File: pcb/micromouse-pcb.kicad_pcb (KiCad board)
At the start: 4 copper layers, 100 x 120 mm, 179 parts, among them J1 BATT_IN_2S, J5 MOTOR_A_N20_ENCODER, J6 MOTOR_B_N20_ENCODER, J7 USB-C rear (GCT USB4105; VBUS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, J8 JTAG_1x6 (3V3,TMS,TCK,TDO,TDI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, J9 BALANCE_2S, Q1 Q_PMOS reverse guard (DMP3098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, Q16 BSS138 (real part; Q_NMOS_GSD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, Q17 BSS138 (real part; Q_NMOS_GSD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, Q18 BSS138 (real part; Q_NMOS_GSD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, Q19 BSS138 (real part; Q_NMOS_GSD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, Q2 PT334-6B (5mm filtered PT; LO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, Q20 BSS138 (real part; Q_NMOS_GSD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, Q21 BSS138 (real part; Q_NMOS_GSD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, Q22 BSS138 (real part; Q_NMOS_GSD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, Q23 BSS138 (real part; Q_NMOS_GSD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, Q24 BSS138 (real part; Q_NMOS_GSD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, Q25 BSS138 (real part; Q_NMOS_GSD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, Q26 BSS138 (real part; Q_NMOS_GSD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, Q27 BSS138 (real part; Q_NMOS_GSD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, Q28 BSS84 (PMOS indicator driver;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, Q29 BSS84 (PMOS indicator driver;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, Q3 PT334-6B (5mm filtered PT; LO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, Q30 BSS84 (PMOS indicator driver;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, Q31 BSS84 (PMOS indicator driver;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, Q32 BSS84 (PMOS indicator driver;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, Q33 BSS84 (PMOS indicator driver;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, Q4 PT334-6B (5mm filtered PT; LO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, Q5 PT334-6B (5mm filtered PT; LO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, Q6 PT334-6B (5mm filtered PT; LO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, Q7 PT334-6B (5mm filtered PT; LO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, SW1 BTN_A (start / BOOT), SW2 RESET, SW3 BTN_B, SW4 BTN_C, SW5 PWR ALL (PCM12SMTR slide; sli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, SW6 PWR MOTORS (PCM12SMTR slide; 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, U1 AP63203WU-7 (fixed 3.3V 2A bu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, U2 TB6612FNG, U3 ESP32-S3-WROOM-1-N8R2 (quad P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, U4 CD74HC4067M, U6 USBLC6-2SC6 (SOT-23-6; 2P6 ba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, U7 TPS54302DDCR (6.0V/3A motor b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, U8 BNO055 (9-axis IMU + fusion; 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

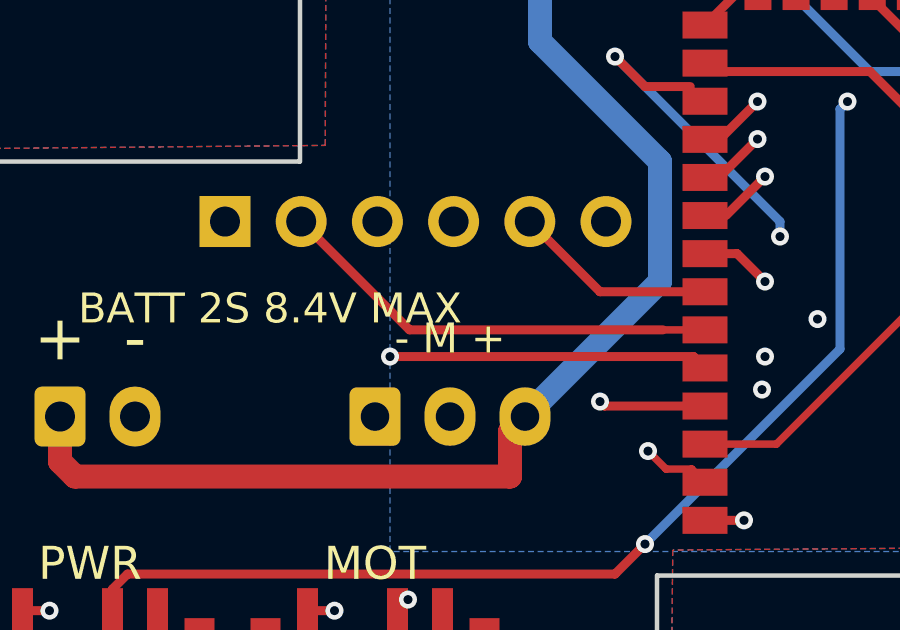
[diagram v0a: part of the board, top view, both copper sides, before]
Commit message: Silk: J9 polarity text clear of BATT label; schematic fuse MPN synced (parity 0)
Co-Authored-By: Claude Opus 4.8 (1M context) <noreply@anthropic.com>
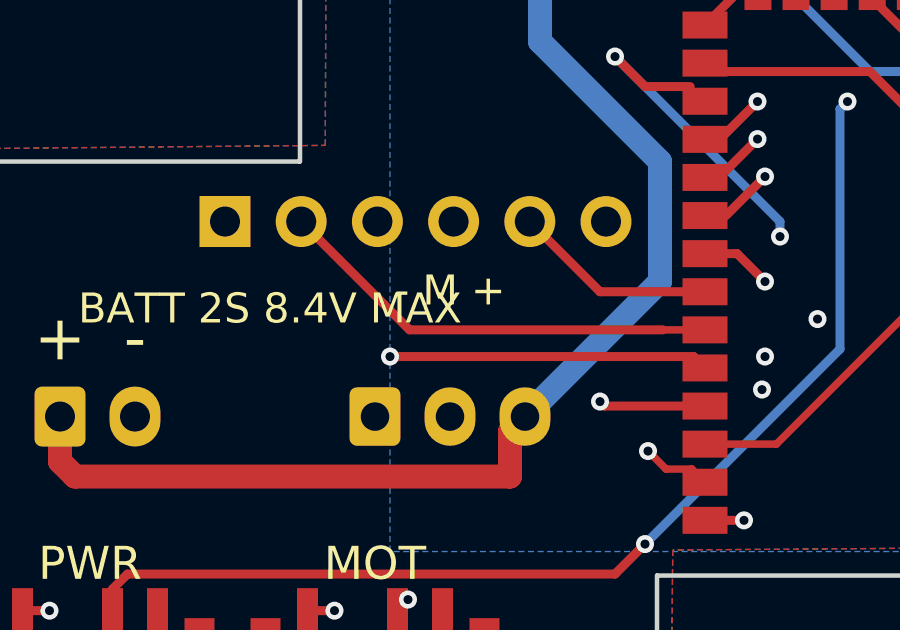
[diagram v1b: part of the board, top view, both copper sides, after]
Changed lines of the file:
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@@
 	)
 	(gr_text "- M +"
-		(at 18 105.9 0)
+		(at 18 104.3 0)
 		(layer "F.SilkS")
 		(effects (font (size 1 1) (thickness 0.2)))

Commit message: Silk: drop the J9 '- M +' text (keyed connector; crowded label zone) -- verify_drc PASS again
Co-Authored-By: Claude Opus 4.8 (1M context) <noreply@anthropic.com>
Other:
- board text removed: "- M +"
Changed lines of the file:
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@@
 		(effects (font (size 1.5 1.5) (thickness 0.3)))
 	)
-	(gr_text "- M +"
-		(at 18 104.3 0)
-		(layer "F.SilkS")
-		(effects (font (size 1 1) (thickness 0.2)))
-	)
 )

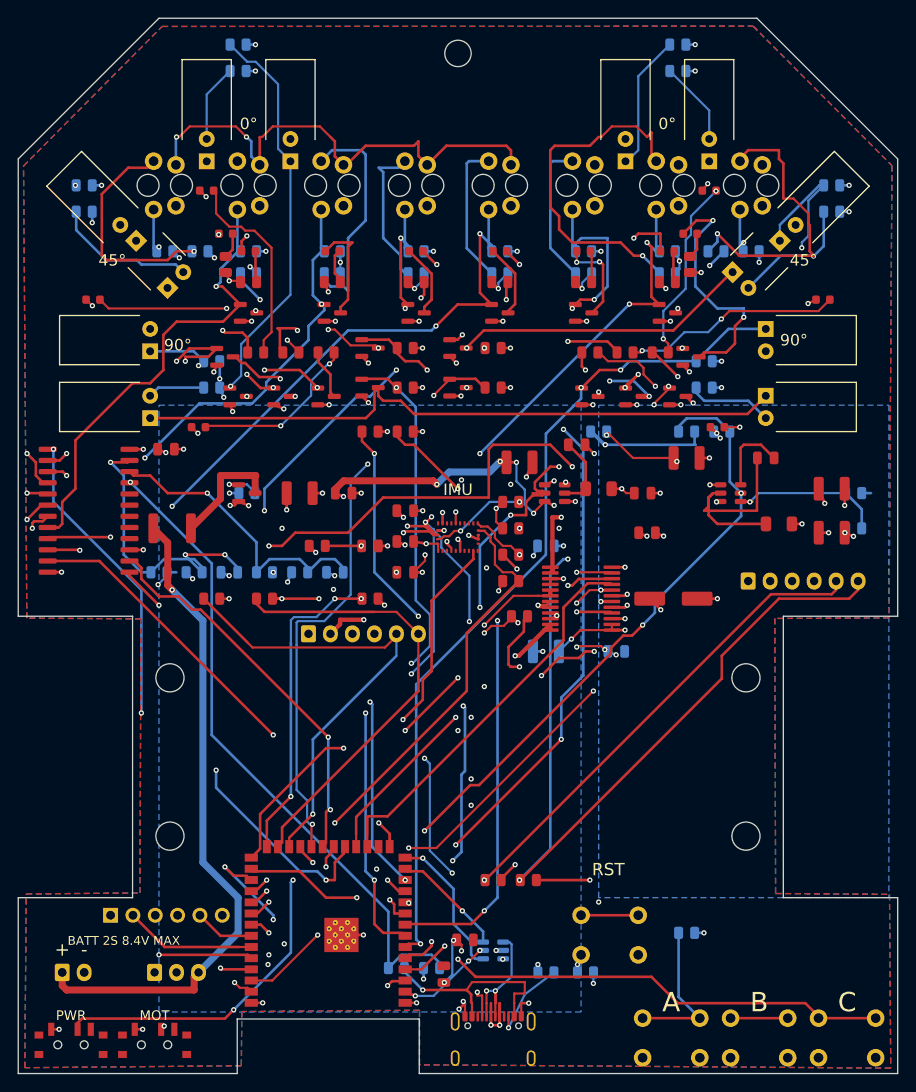
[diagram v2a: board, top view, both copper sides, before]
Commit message: Rev 7.2: XT60 + buzzer + ZH direct-plug motors + IMU self-test -- verify_drc 0/0, 12/12 battery, dual fab packages
User work order (HANDOFF 18) + same-day requests, all closed:
- J10 AMASS XT60-M (male) battery input in PARALLEL with J1 JST-XH:
  rear-right shelf placement via hole-aware free-rect scan against the
  true Edge.Cuts polygon with optical-corridor keepouts (two earlier
  candidate spots rejected with evidence: outline void / line-array
  through-holes). 0.8mm BATT_RAW feed; '+'/'-' + ONE PACK ONLY silk;
  normal BOM line (Lion procures; hand-fit fallback documented).
- BZ1 buzzer (CMT-8504, 15R coil) on IO46 via R81 220R -> Q34 MMBT2222A
  + D29 1N4148W flyback; strap-safe (load only ever pulls the boot strap
  low). fw beep API: ready/run/stop/low-batt/stall/IMU-fail chirps.
- J5/J6 -> JST ZH B6B-ZR in the robu GA12-N20 factory-cable order
  (M1,VCC,C1,C2,GND,M2): motor plugs straight in, zero soldering.
  Meter-check VCC/GND (pins 2/5) once before first plug-in.
- J9 balance lead now OPTIONAL: fw auto-detects (BAT_MID_SENSE ~0V) and
  falls back to the 6.6V pack floor.
- IMU functioning checks: sim_preflight I1-I6 (bus topology, Fast-mode
  timing, straps, reset pull-ups, CAP, INT, register audit) + boot
  self-test in fw (CHIP_ID, POST, fusion status; 4-chirp on failure).
- Sims updated to the exact ordered motor (600 ticks/rev, 200RPM, 43mm
  wheel, 0.23A stall); 8.4V question closed: motors sit on the regulated
  6.00V rail (circuit_tests M2/M3).
- Selective silk refdes for 23 debug-critical parts (clear-spot scanner
  seeded against board labels) + assembly-top/bottom.pdf debug maps
  (new export_fab gate). Project-local 3D models for ZH + buzzer.
- Production folders (pcb/tools/export_release.py): fab_release/
  lion-circuits/ (gerber zip + BOM + pos + assembly PDFs + ORDERING.md)
  and fab_release/jlcpcb/ (flat gerber+drill zip, JLC-format BOM/CPL,
  ORDERING.md with LCSC/rotation/origin caveats).
- Full Lion stock re-sweep 2026-07-19/20: every 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
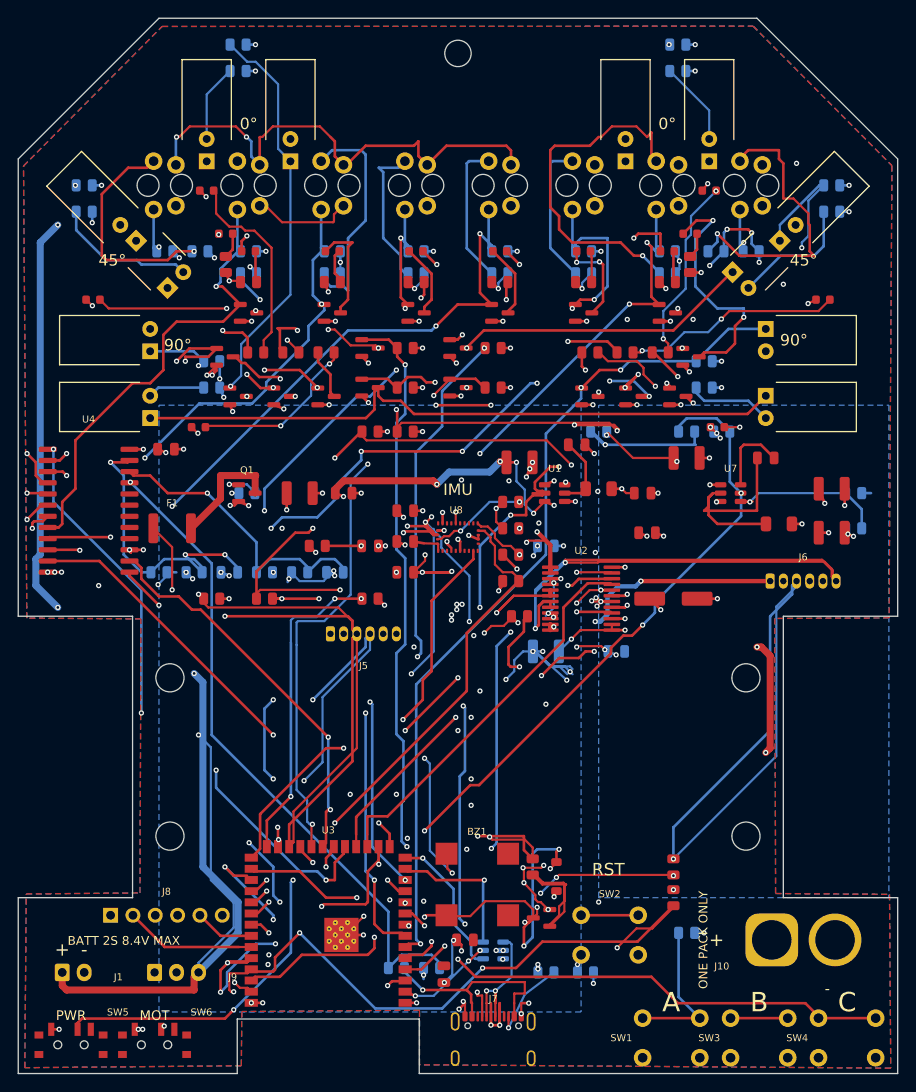
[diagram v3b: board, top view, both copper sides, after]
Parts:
- added BZ1: CMT-8504-100-SMT (magnetic transducer 8.5mm, 15R coil, 4kHz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, Buzzer_Beeper:MagneticBuzzer_CUI_CMT-8504-100-SMT, F.Cu at (52.2, 98.5)
- added D29: 1N4148W (flyback clamp across the buzzer coil), Diode_SMD:D_SOD-123, F.Cu at (61.2, 97.6)
- added J10: BATT_IN_XT60 (parallel option -- ONE PACK ONLY), Connector_AMASS:AMASS_XT60-M_1x02_P7.20mm_Vertical, F.Cu at (85.7, 104.8)
- added Q34: MMBT2222A (buzzer low-side driver; Q_NPN_BEC base symbol so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, Package_TO_SOT_SMD:SOT-23, F.Cu at (59.5, 102.3)
- added R81: 220, Resistor_SMD:R_0805_2012Metric, F.Cu at (58.5, 96.5)
- J5, J6: footprint Connector_JST:JST_XH_B6B-XH-A_1x06_P2.50mm_Vertical -> Connector_JST:JST_ZH_B6B-ZR_1x06_P1.50mm_Vertical
- moved R57 20.6 mm to (74.5, 96.5), turned to -90 degrees
- moved R58 16.6 mm to (74.5, 100.0), turned to -90 degrees
- moved J5 2.50 mm to (35.5, 70.0)
- moved J6 2.50 mm to (85.5, 64.0)
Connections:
- J5 pad 2: MOTA_N -> PLUS3V3
- J5 pad 3: PLUS3V3 -> ENC1_A
- J5 pad 4: GND -> ENC1_B
- J5 pad 5: ENC1_A -> GND
- J5 pad 6: ENC1_B -> MOTA_N
- J6 pad 2: MOTB_N -> PLUS3V3
- J6 pad 3: PLUS3V3 -> ENC2_A
- J6 pad 4: GND -> ENC2_B
- J6 pad 5: ENC2_A -> GND
- J6 pad 6: ENC2_B -> MOTB_N
- U3 pad 16: unconnected-(U3-IO46-Pad16) -> BUZZ_CTRL
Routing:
- net BATT_RAW: track 75.3 -> 364.0 mm, vias 1 -> 8
- net ENC2_A_S3: track 60.3 -> 290.2 mm, vias 4 -> 15
- net GND: track 105.4 -> 235.8 mm, vias 73 -> 112
- net ENC2_A: track 111.8 -> 215.1 mm, vias 4 -> 7
- net ENC2_B: track 119.5 -> 200.2 mm, vias 3 -> 6
- net BUZZ_CTRL: track 0.00 -> 76.1 mm, vias 0 -> 7
- net MOTB_N: track 35.9 -> 93.6 mm, vias 1 -> 2
- net BUZZ_DRV: track 0.00 -> 54.1 mm, vias 0 -> 6
- net ENC1_B: track 51.2 -> 103.9 mm, vias 0 -> 8
- net ENC1_A: track 54.2 -> 95.9 mm, vias 1 -> 2
- net ENC2_B_S3: track 160.4 -> 120.1 mm
- net MOTA_P: track 44.5 -> 73.6 mm, vias 3 -> 2
- net MOTB_P: track 39.2 -> 58.8 mm, vias 1 -> 3
- net Net-(Q34-B): track 0.00 -> 19.3 mm
- net PLUS3V3: track 227.1 -> 245.9 mm, vias 76 -> 79
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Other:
- board text added: "ONE PACK ONLY"
